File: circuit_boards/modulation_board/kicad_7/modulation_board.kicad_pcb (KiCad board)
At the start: 4 copper layers, 111.8 x 165.1 mm, 244 parts, among them J1 MOD_BOARD_EXT_CON, J2 VCO_BOARD_CON, J3 VCF_BOARD_CON, J301 SWD_header, J4 power_entry, Q501 MMBT3904, Q801 MMBT3904, SW301 5511M12, SW501 E-Switch_EG2301B, SW502 E-Switch_EG2301B, SW503 E-Switch_EG2301B, SW504 E-Switch_EG2301B, SW505 E-Switch_EG2301B, SW506 E-Switch_EG2301B, SW507 E-Switch_EG2301B, SW801 E-Switch_EG2301B, SW802 SR1712F-0204, U1 STM32L412K8Ux, U10 TL072, U1001 L78L05_SOT89, U1002 L79L05_SOT89, U1003 L78L33_SOT89, U11 74HC595, U12 SSI2130, U13 TL072, U14 TL072, U15 MCP6002-xSN, U2 VO0600T, U3 SN74LV1T34DBV, U4 LM4040C-2.5, U5 74HC4067PW, U6 74HC4067PW, U7 MCP6002-xSN, U8 DAC8162xDGSx, U801 LM4040C-2.5, U9 DAC128S085CIMT, Y301 32_768KHZ

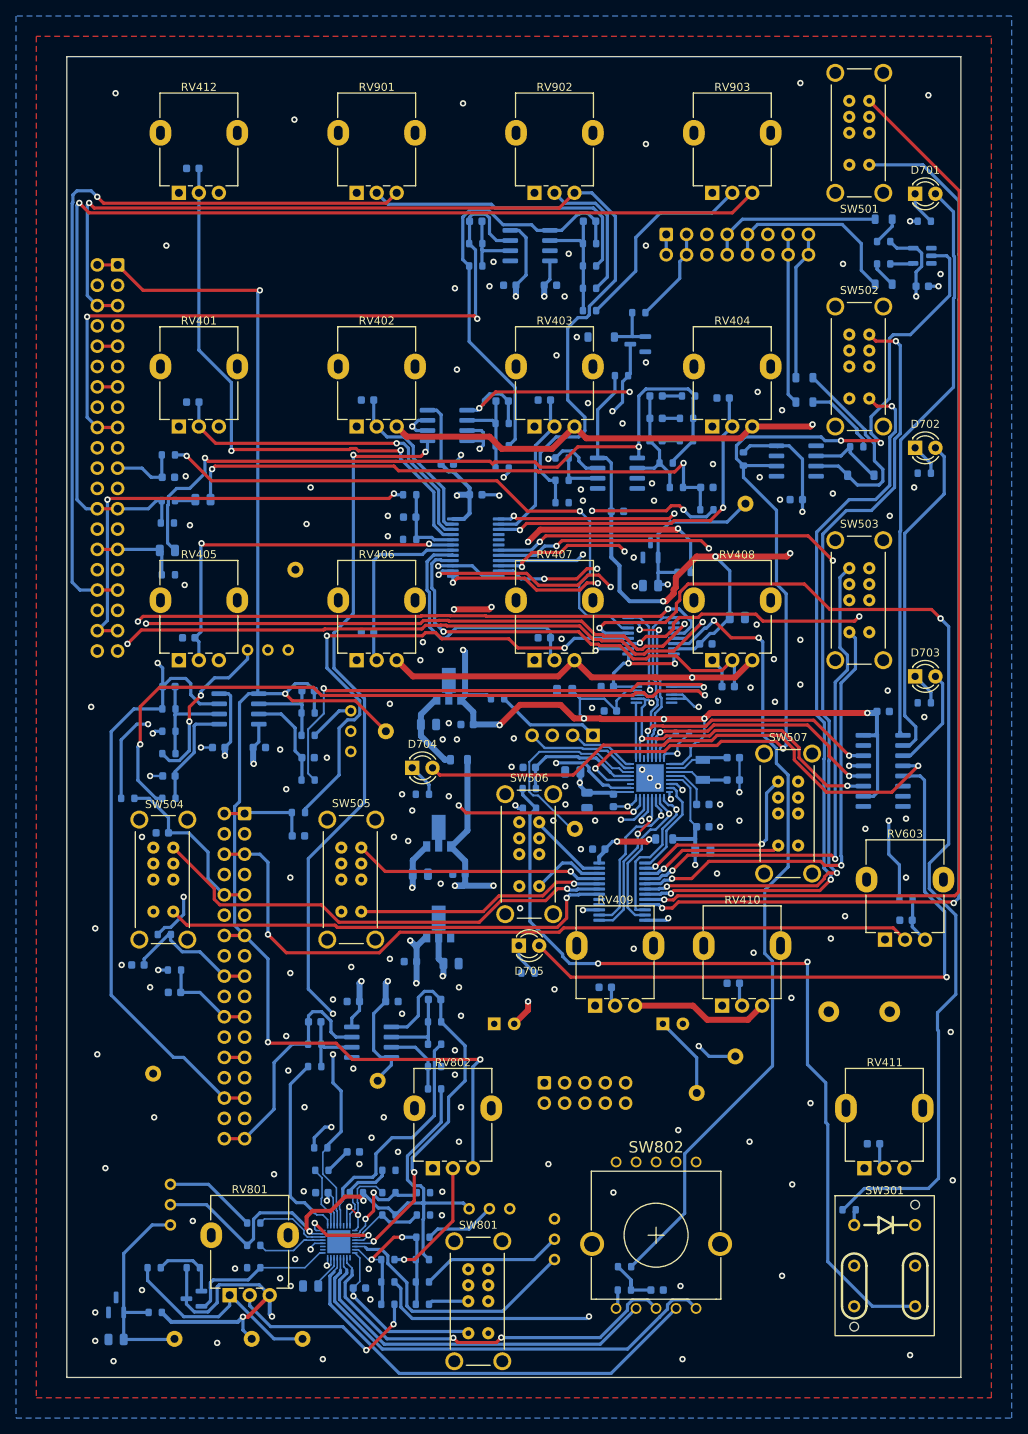
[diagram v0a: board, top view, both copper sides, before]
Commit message: Add potentiometer 3d model to VCO and MOD boards
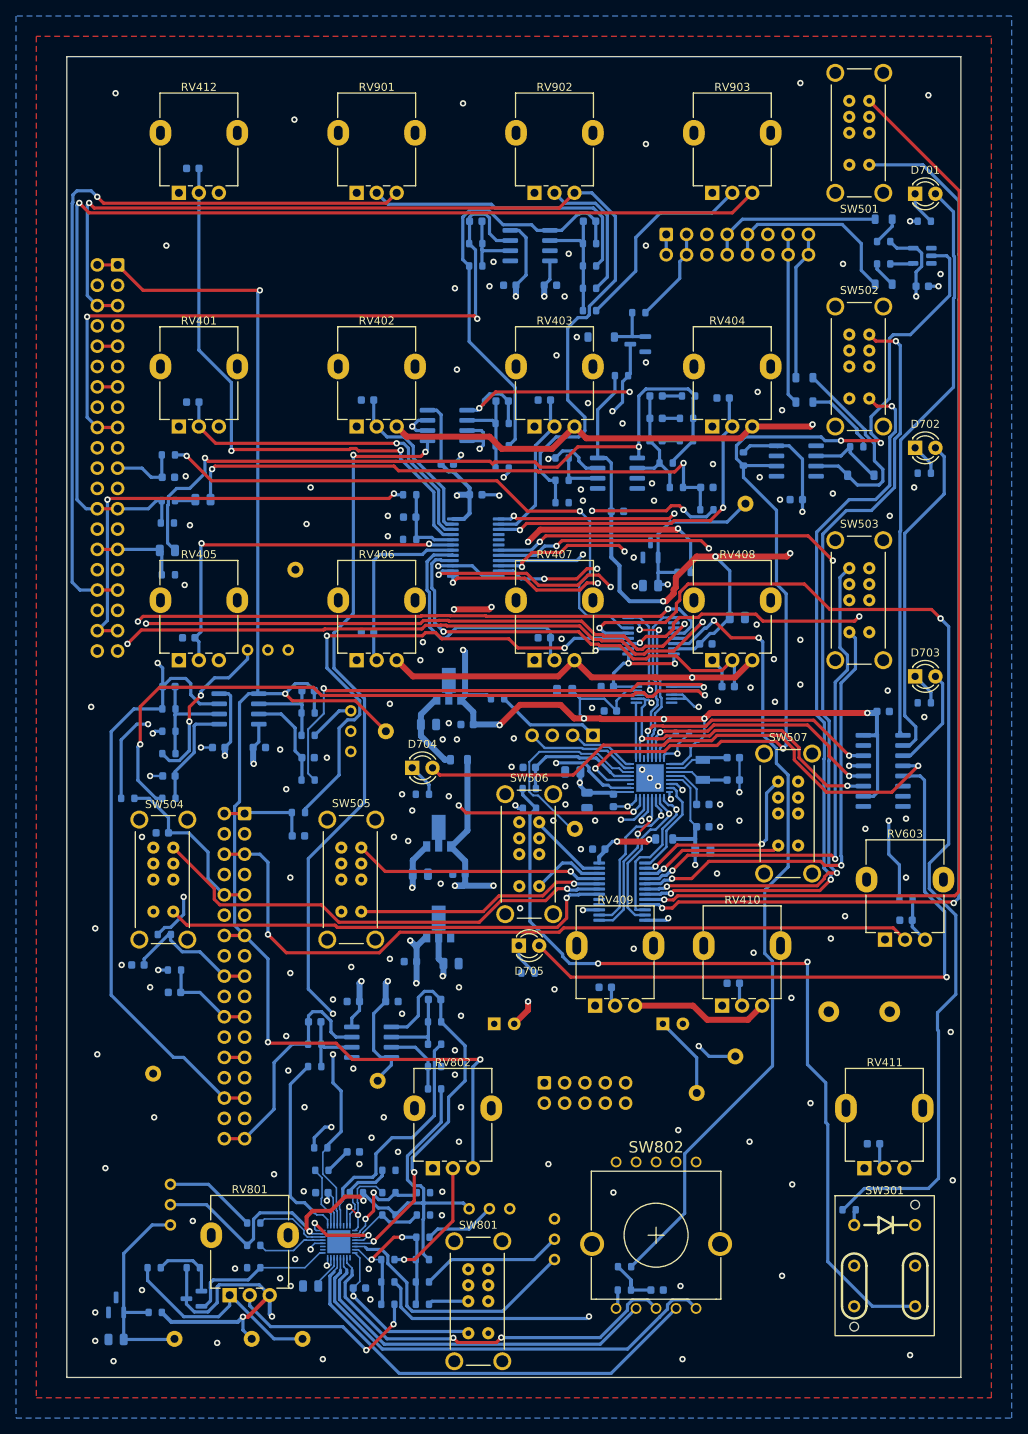
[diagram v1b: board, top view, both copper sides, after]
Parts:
- RV401, RV402, RV403, RV404, RV405, RV406, RV407, RV408, RV412, RV603, RV801, RV802, RV901, RV902, RV903: footprint Potentiometer_THT:Potentiometer_Alpha_RD901F-40-00D_Single_Vertical -> custom_footprints:Potentiometer_Alpha_RD901F-40-00D_Single_Vertical
